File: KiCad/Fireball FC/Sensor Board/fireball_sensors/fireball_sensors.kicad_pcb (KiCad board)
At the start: 2 copper layers, 36.3 x 31.8 mm, 29 parts, among them J5 Conn_01x06, M1 MountingHole_2.2mm_M2, M2 MountingHole_2.2mm_M2, M3 MountingHole_2.2mm_M2, M4 MountingHole_2.2mm_M2, SW2 MAIN POWER, U2 MAX17048G, U3 TPS61023, U5 NCP708, U8 LSM6DSO, U9 MS5607-02BA

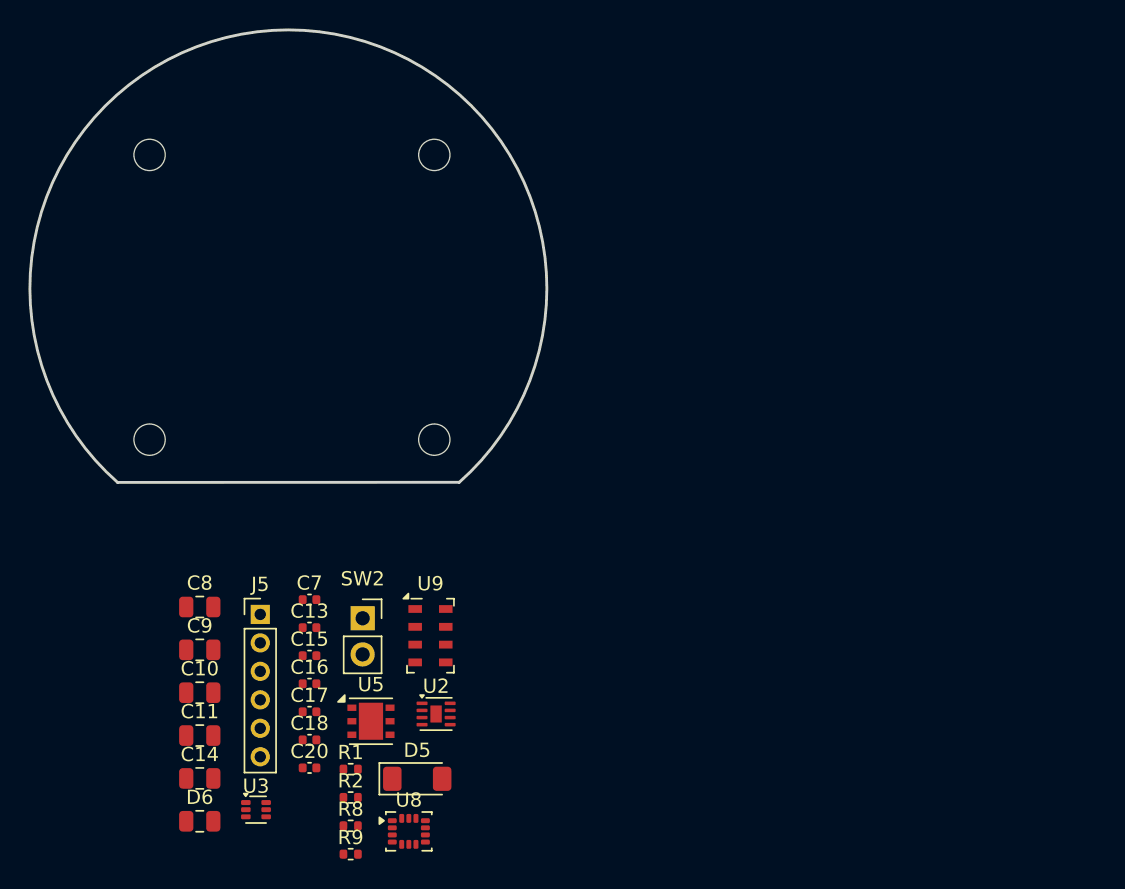
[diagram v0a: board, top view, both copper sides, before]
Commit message: Layout for sensor board done. Still need to add silkscreen art
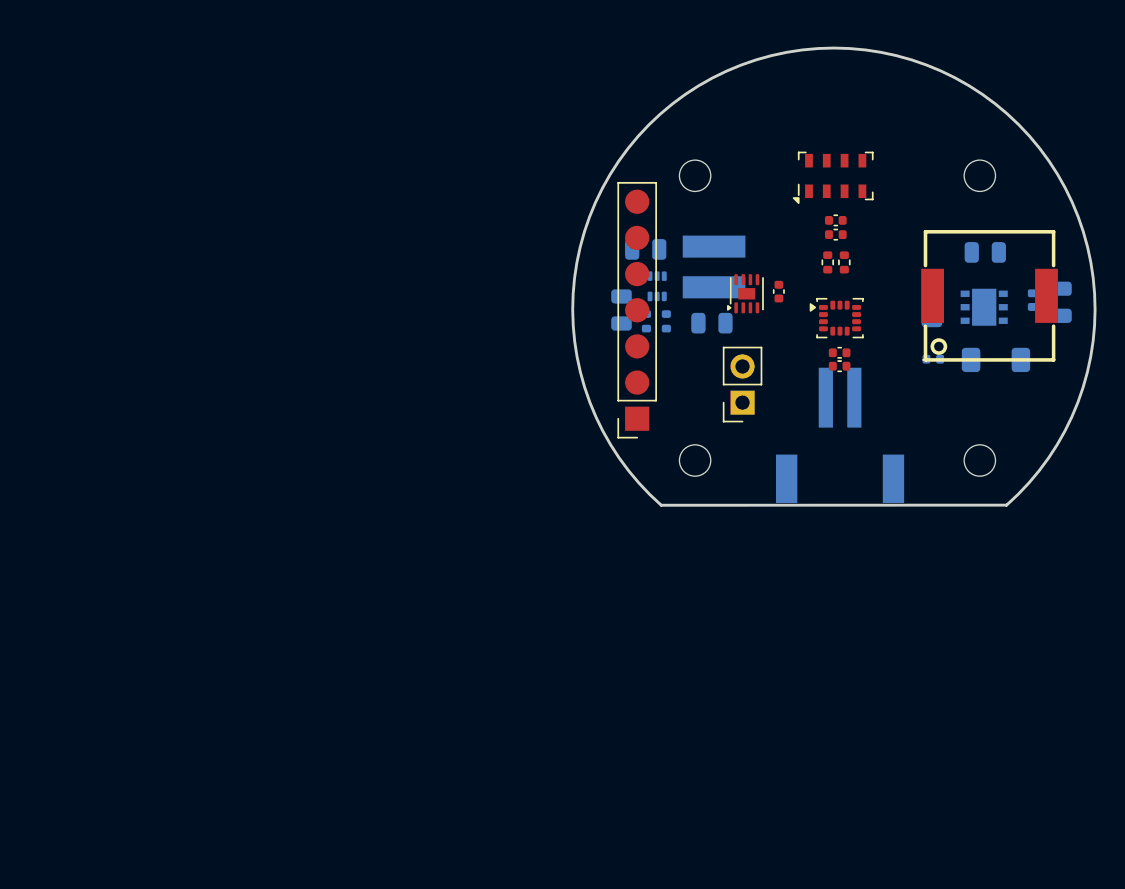
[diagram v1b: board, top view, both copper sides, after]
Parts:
- removed J5: Conn_01x06, Connector_PinHeader_2.00mm:PinHeader_1x06_P2.00mm_Vertical
- added BUZ1: CPT-9019S-SMT-TR, lcsc_footprints:C95163_BUZ-SMD_L9_0-W9_0-P8_00-LS9_3, F.Cu at (243.8, 64.2)
- added CN1: HDGC2001WR-S-2P, lcsc_footprints:C2936224_CONN-SMD_2P-P2_00_HDGC_HDGC2001WR-S-2P, B.Cu at (233.3, 74.2)
- added J1: Conn_01x07, Connector_PinSocket_2.54mm:PinSocket_1x07_P2.54mm_Vertical, F.Cu at (219.1, 72.8)
- added L2: FTC404030S1R0MGCA, lcsc_footprints:C39676079_IND-SMD_L4_1-W4_1_SPM40XX, B.Cu at (224.4, 62.2)
- C10, C11, C13, C14, C15, C8, C9, D5, D6, R1, R2, U3, U5: moved to B.Cu
- moved D6 70.7 mm to (248.8, 64.7), turned to 90 degrees
- moved C14 66.4 mm to (243.5, 61.1), turned to 180 degrees
- moved C11 59.6 mm to (239.8, 65.0), turned to 90 degrees
- moved C15 56.6 mm to (246.8, 64.5), turned to 90 degrees
- moved R9 54.1 mm to (233.6, 61.9), turned to 90 degrees
- moved U5 52.0 mm to (243.4, 65.0), turned to 180 degrees
- moved R8 51.9 mm to (232.4, 61.9), turned to 90 degrees
- moved C17 50.6 mm to (233.0, 58.9), turned to 180 degrees
- moved D5 50.2 mm to (244.2, 68.7)
- moved C16 48.6 mm to (233.0, 59.9), turned to 180 degrees
- moved C13 47.7 mm to (239.8, 68.7), turned to 180 degrees
- moved U8 47.1 mm to (233.3, 65.8)
- moved C20 46.7 mm to (233.3, 69.1)
- moved U3 46.3 mm to (220.4, 63.5), turned to 90 degrees
- moved C18 46.1 mm to (233.3, 68.2)
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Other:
- board size 36.3 x 31.8 mm -> 36.7 x 32.1 mm

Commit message: routing :D (help)
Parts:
- added D1: LED_Small, LED_SMD:LED_0805_2012Metric, F.Cu at (238.0, 71.3)
- added R3: R_Small, Resistor_SMD:R_0402_1005Metric, F.Cu at (238.5, 73.6)
- C10, C11, C13, C15, C8, C9, D5, D6, R1, U3, U5: moved to F.Cu
- C7, J1: moved to B.Cu
- moved D6 29.3 mm to (220.0, 69.8), turned to 0 degrees
- moved D5 25.9 mm to (219.2, 61.8), turned to 90 degrees
- moved C15 20.8 mm to (226.0, 63.0), turned to 180 degrees
- moved U5 20.5 mm to (223.2, 62.1)
- moved C13 20.4 mm to (221.8, 59.1), turned to -90 degrees
- moved C14 18.0 mm to (225.5, 62.0), turned to 90 degrees
- moved C11 14.7 mm to (226.2, 59.2), turned to 0 degrees
- moved U2 8.02 mm to (233.7, 68.0), turned to 0 degrees
- moved C16 8.00 mm to (231.8, 52.0), turned to 0 degrees
- moved C8 7.66 mm to (229.8, 71.5), turned to 90 degrees
- moved U3 6.52 mm to (226.2, 66.5), turned to 60 degrees
- moved C17 6.03 mm to (231.8, 53.0), turned to 0 degrees
- moved R1 5.98 mm to (225.5, 64.5), turned to 180 degrees
- moved L2 5.70 mm to (229.9, 63.8), turned to 180 degrees
- moved C7 5.57 mm to (226.2, 68.7), turned to 150 degrees
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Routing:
- net /SCL: track 0.00 -> 42.6 mm, vias 0 -> 3
- net /SDA: track 0.00 -> 41.9 mm, vias 0 -> 3
- net GND: track 0.00 -> 39.9 mm, vias 0 -> 15
- net /BUZZER: track 0.00 -> 34.0 mm, vias 0 -> 3
- net +BATT: track 0.00 -> 25.1 mm, vias 0 -> 2
- net /5V_EN: track 0.00 -> 24.8 mm, vias 0 -> 3
- net +5V: track 0.00 -> 19.2 mm, vias 0 -> 4
- net Net-(SW2-A): track 0.00 -> 6.42 mm
- net Net-(U3-SW): track 0.00 -> 3.17 mm, vias 0 -> 1
- net +3V3: track 0.00 -> 1.98 mm, vias 0 -> 1
- net Net-(D1-A): track 0.00 -> 1.40 mm
- net Net-(U3-VOUT): track 0.00 -> 1.20 mm
- added copper zone on F.Cu, net +3V3
- added copper zone on B.Cu, net GND

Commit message: update silkscreen
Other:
- board text added: "fireball sensor board"
- board text added: "v1-by @icechez @sjacksonhodum"
